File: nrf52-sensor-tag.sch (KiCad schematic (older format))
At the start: 21 parts, among them IC1 ISP1807-LR-RS, IC2 MAX44009EDT+T, J1 Conn_01x06_Male, U1 BME280

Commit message: Finalized layout
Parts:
- removed J1: Conn_01x06_Male, Connector_PinHeader_2.00mm:PinHeader_1x06_P2.00mm_Vertical, symbol Connector:Conn_01x06_Male
- added J3: Conn_01x07_Male, Connector_PinHeader_2.54mm:PinHeader_1x07_P2.54mm_Vertical, symbol Connector:Conn_01x07_Male
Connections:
- net GND: now also J3.4 (Pin_4), J3.5 (Pin_5)
- net Rx: now also J3.6 (Pin_6)
- net SWDCLK: now also J3.1 (Pin_1)
- net SWDIO: now also J3.2 (Pin_2)
- net Tx: now also J3.7 (Pin_7)
- net VCC: now also J3.3 (Pin_3)
- no-connect marks 35 -> 40
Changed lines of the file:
@@
 $EndDescr
-$Comp
-L ISP1807-LR-RS:ISP1807-LR-RS IC1
-U 1 1 601E6B9F
-P 1550 1400
-F 0 "IC1" H 2750 1700 50  0000 C CNN
-F 1 "ISP1807-LR-RS" H 2750 1600 50  0000 C CNN
-F 2 "ISP1807:ISP1807LRRS" H 3700 1500 50  0001 L CNN
-F 3 "https://www.insightsip.com/fichiers_insightsip/pdf/ble/ISP1807/isp_ble_DS1807.pdf" H 3700 1400 50  0001 L CNN
-F 4 "RX TXRX MODULE BT TRC ANT SMD" H 3700 1300 50  0001 L CNN "Description"
-F 5 "1" H 3700 1200 50  0001 L CNN "Height"
-F 6 "Insight SIP" H 3700 1100 50  0001 L CNN "Manufacturer_Name"
-F 7 "ISP1807-LR-RS" H 3700 1000 50  0001 L CNN "Manufacturer_Part_Number"
-F 8 "359-ISP1807-LR-RS" H 3700 900 50  0001 L CNN "Mouser Part Number"
-F 9 "https://www.mouser.co.uk/ProductDetail/Insight-SiP/ISP1807-LR-RS?qs=PqoDHHvF649jBaTuCZQSOQ%3D%3D" H 3700 800 50  0001 L CNN "Mouser Price/Stock"
-F 10 "" H 3700 700 50  0001 L CNN "Arrow Part Number"
-F 11 "" H 3700 600 50  0001 L CNN "Arrow Price/Stock"
-	1    1550 1400
-	1    0    0    -1
-$EndComp
 $Comp
 L power:GND #PWR0101
 U 1 1 6021B8C4
-P 2700 6800
-F 0 "#PWR0101" H 2700 6550 50  0001 C CNN
-F 1 "GND" H 2705 6627 50  0000 C CNN
-F 2 "" H 2700 6800 50  0001 C CNN
-F 3 "" H 2700 6800 50  0001 C CNN
-	1    2700 6800
+P 2700 6850
+F 0 "#PWR0101" H 2700 6600 50  0001 C CNN
+F 1 "GND" H 2705 6677 50  0000 C CNN
+F 2 "" H 2700 6850 50  0001 C CNN
+F 3 "" H 2700 6850 50  0001 C CNN
+	1    2700 6850
 	1    0    0    -1
 $EndComp
@@
 L power:GND #PWR0102
 U 1 1 6020BA24
-P 8600 2550
-F 0 "#PWR0102" H 8600 2300 50  0001 C CNN
-F 1 "GND" H 8605 2377 50  0000 C CNN
-F 2 "" H 8600 2550 50  0001 C CNN
-F 3 "" H 8600 2550 50  0001 C CNN
-	1    8600 2550
+P 8600 2600
+F 0 "#PWR0102" H 8600 2350 50  0001 C CNN
+F 1 "GND" H 8605 2427 50  0000 C CNN
+F 2 "" H 8600 2600 50  0001 C CNN
+F 3 "" H 8600 2600 50  0001 C CNN
+	1    8600 2600
 	1    0    0    -1
 $EndComp
@@
 L power:GND #PWR0103
 U 1 1 6020C669
-P 8800 2550
-F 0 "#PWR0103" H 8800 2300 50  0001 C CNN
-F 1 "GND" H 8805 2377 50  0000 C CNN
-F 2 "" H 8800 2550 50  0001 C CNN
-F 3 "" H 8800 2550 50  0001 C CNN
-	1    8800 2550
+P 8800 2600
+F 0 "#PWR0103" H 8800 2350 50  0001 C CNN
+F 1 "GND" H 8805 2427 50  0000 C CNN
+F 2 "" H 8800 2600 50  0001 C CNN
+F 3 "" H 8800 2600 50  0001 C CNN
+	1    8800 2600
 	1    0    0    -1
 $EndComp
@@
 $EndComp
 Wire Wire Line
-	8600 1300 8800 1300
+	8600 1300 8700 1300
 Wire Wire Line
 	8800 1300 9600 1300
@@
 Connection ~ 8150 4900
 Wire Wire Line
-	8150 4900 8750 4900
+	8150 4900 8450 4900
 NoConn ~ 3850 1500
 NoConn ~ 3850 1700
@@
 Wire Wire Line
 	9600 1300 9900 1300
-$Comp
-L Connector:Conn_01x06_Male J1
-U 1 1 6020A1D2
-P 5200 6650
-F 0 "J1" H 5308 7031 50  0000 C CNN
-F 1 "Conn_01x06_Male" H 5308 6940 50  0000 C CNN
-F 2 "Connector_PinHeader_2.00mm:PinHeader_1x06_P2.00mm_Vertical" H 5200 6650 50  0001 C CNN
-F 3 "~" H 5200 6650 50  0001 C CNN
-	1    5200 6650
-	1    0    0    -1
-$EndComp
 Text Label 5800 6550 2    50   ~ 0
 SWDIO
@@
 $EndComp
 Wire Wire Line
-	5400 6750 6000 6750
+	5400 6750 5500 6750
 Wire Wire Line
 	5800 6650 5400 6650
@@
 Wire Wire Line
 	6000 6800 6000 6750
+Text Label 5800 7050 2    50   ~ 0
+Tx
 Text Label 5800 6950 2    50   ~ 0
-Tx
-Text Label 5800 6850 2    50   ~ 0
 Rx
 Wire Wire Line
-	5800 6850 5400 6850
-Wire Wire Line
 	5800 6950 5400 6950
+Wire Wire Line
+	5800 7050 5400 7050
 Text Label 4400 2600 2    50   ~ 0
 Rx
@@
 	4400 2800 3850 2800
 Wire Wire Line
-	1400 950  2350 950
+	1400 950  2050 950
 Connection ~ 1400 950
 Wire Notes Line
@@
 Text Notes 600  650  0    50   ~ 0
 ISP1807 (nRF52) µC
+$Comp
+L Connector:Conn_01x07_Male J3
+U 1 1 6021CB85
+P 5200 6750
+F 0 "J3" H 5308 7231 50  0000 C CNN
+F 1 "Conn_01x07_Male" H 5308 7140 50  0000 C CNN
+F 2 "Connector_PinHeader_2.54mm:PinHeader_1x07_P2.54mm_Vertical" H 5200 6750 50  0001 C CNN
+F 3 "~" H 5200 6750 50  0001 C CNN
+	1    5200 6750
+	1    0    0    -1
+$EndComp
+Wire Wire Line
+	5400 6850 5500 6850
+Wire Wire Line
+	5500 6850 5500 6750
+Connection ~ 5500 6750
+Wire Wire Line
+	5500 6750 6000 6750
+NoConn ~ 4400 1400
+NoConn ~ 4400 1600
+NoConn ~ 1200 1800
+NoConn ~ 1200 1900
+NoConn ~ 1200 2000
+$Comp
+L power:PWR_FLAG #FLG0101
+U 1 1 6029FC8F
+P 2050 950
+F 0 "#FLG0101" H 2050 1025 50  0001 C CNN
+F 1 "PWR_FLAG" H 2050 1123 50  0000 C CNN
+F 2 "" H 2050 950 50  0001 C CNN
+F 3 "~" H 2050 950 50  0001 C CNN
+	1    2050 950
+	1    0    0    -1
+$EndComp
+Connection ~ 2050 950
+Wire Wire Line
+	2050 950  2350 950
+$Comp
+L power:PWR_FLAG #FLG0102
+U 1 1 602A143F
+P 8450 4900
+F 0 "#FLG0102" H 8450 4975 50  0001 C CNN
+F 1 "PWR_FLAG" H 8450 5073 50  0000 C CNN
+F 2 "" H 8450 4900 50  0001 C CNN
+F 3 "~" H 8450 4900 50  0001 C CNN
+	1    8450 4900
+	1    0    0    -1
+$EndComp
+Connection ~ 8450 4900
+Wire Wire Line
+	8450 4900 8750 4900
+$Comp
+L power:PWR_FLAG #FLG0103
+U 1 1 602A1E76
+P 8700 1300
+F 0 "#FLG0103" H 8700 1375 50  0001 C CNN
+F 1 "PWR_FLAG" H 8700 1473 50  0000 C CNN
+F 2 "" H 8700 1300 50  0001 C CNN
+F 3 "~" H 8700 1300 50  0001 C CNN
+	1    8700 1300
+	1    0    0    -1
+$EndComp
+Connection ~ 8700 1300
+Wire Wire Line
+	8700 1300 8800 1300
+Wire Wire Line
+	8600 2550 8600 2600
+Wire Wire Line
+	8800 2550 8800 2600
+Wire Wire Line
+	2700 6850 2700 6800
+$Comp
+L ISP1807-LR-RS:ISP1807-LR-RS IC1
+U 1 1 601E6B9F
+P 1550 1400
+F 0 "IC1" H 2750 1700 50  0000 C CNN
+F 1 "ISP1807-LR-RS" H 2750 1600 50  0000 C CNN
+F 2 "ISP1807:ISP1807LRRS" H 3700 1500 50  0001 L CNN
+F 3 "https://www.insightsip.com/fichiers_insightsip/pdf/ble/ISP1807/isp_ble_DS1807.pdf" H 3700 1400 50  0001 L CNN
+F 4 "RX TXRX MODULE BT TRC ANT SMD" H 3700 1300 50  0001 L CNN "Description"
+F 5 "1" H 3700 1200 50  0001 L CNN "Height"
+F 6 "Insight SIP" H 3700 1100 50  0001 L CNN "Manufacturer_Name"
+F 7 "ISP1807-LR-RS" H 3700 1000 50  0001 L CNN "Manufacturer_Part_Number"
+F 8 "359-ISP1807-LR-RS" H 3700 900 50  0001 L CNN "Mouser Part Number"
+F 9 "https://www.mouser.co.uk/ProductDetail/Insight-SiP/ISP1807-LR-RS?qs=PqoDHHvF649jBaTuCZQSOQ%3D%3D" H 3700 800 50  0001 L CNN "Mouser Price/Stock"
+F 10 "" H 3700 700 50  0001 L CNN "Arrow Part Number"
+F 11 "" H 3700 600 50  0001 L CNN "Arrow Price/Stock"
+	1    1550 1400
+	1    0    0    -1
+$EndComp
 $EndSCHEMATC

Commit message: Add new alternative sensors
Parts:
- removed IC2: MAX44009EDT+T, MAX44009EDT+T:SON65P200X200X65-7N-D, symbol MAX44009EDT+T:MAX44009EDT+T
- removed U1: BME280, Package_LGA:Bosch_LGA-8_2.5x2.5mm_P0.65mm_ClockwisePinNumbering, symbol Sensor:BME280
- added IC2: VEML6030, VEML6030:VEML6030, symbol VEML6030:VEML6030
- added IC3: MS860702BA01-50, MS860702BA01-50:SON125P300X500X100-8N, symbol MS860702BA01-50:MS860702BA01-50
- added R5: 10R, Resistor_SMD:R_0603_1608Metric, symbol Device:R_Small
- C5: value 0.1uF -> 0.22uF
- C6: value 0.1uF -> 10uF
- C8: value 1uF -> 0.1uF
- R1, R2: value 10k -> 4.7k
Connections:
- net GND: now also IC2.1 (GND), IC3.3 (GND)
- net SCL: now also IC2.5 (SCL), IC3.8 (SCL)
- net SDA: now also IC2.2 (SDA), IC3.7 (SDA)
- net ~INT1: no longer R3.2
- net BME280_VCC renamed SENS1_VCC
- net SENS1_VCC: now also IC3.1 (VDD); no longer C6.1
- net MAX44_VCC renamed SENS2_VCC
- net SENS2_VCC: now also C6.1, R5.1
- new net: IC2.4 (ADD), IC2.6 (VDD), R5.2
- new net INT1: IC2.3 (INT), R3.2
- no-connect marks 40 -> 44
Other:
- note added: "Humid, Temp, Pressure"
- note added: "I2C Address Pressure + Temp: 0x76"
- note added: "I2C Address Relative Humidity: 0x40"
- note added: "I2C Address: 0x48"
- note added: "Light Sensor"
- note removed: "1001010x"
- note removed: "BME280 Humid, Temp, Presure"
- note removed: "I2C Address: 0x4A"
- note removed: "I2C Address: 0x76"
- note removed: "MAX44009 Light Sensor"
- moved on the sheet: JP1, JP2

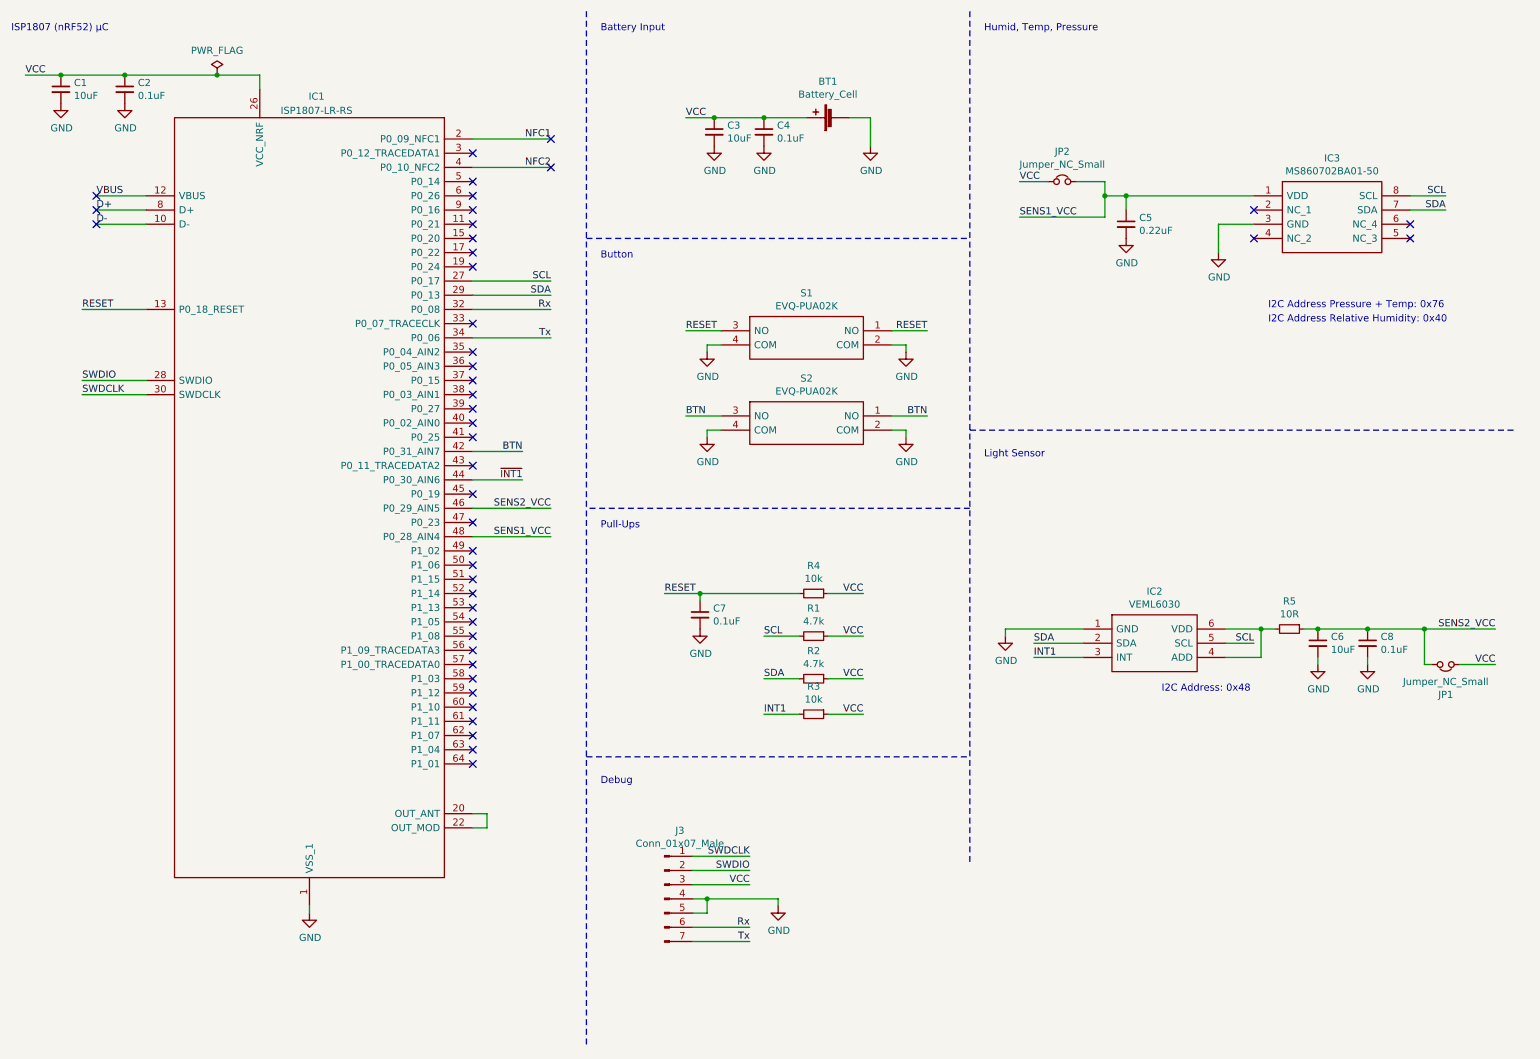
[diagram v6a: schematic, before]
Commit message: Add MS88SF2 nRF52 Module and re-arranged components
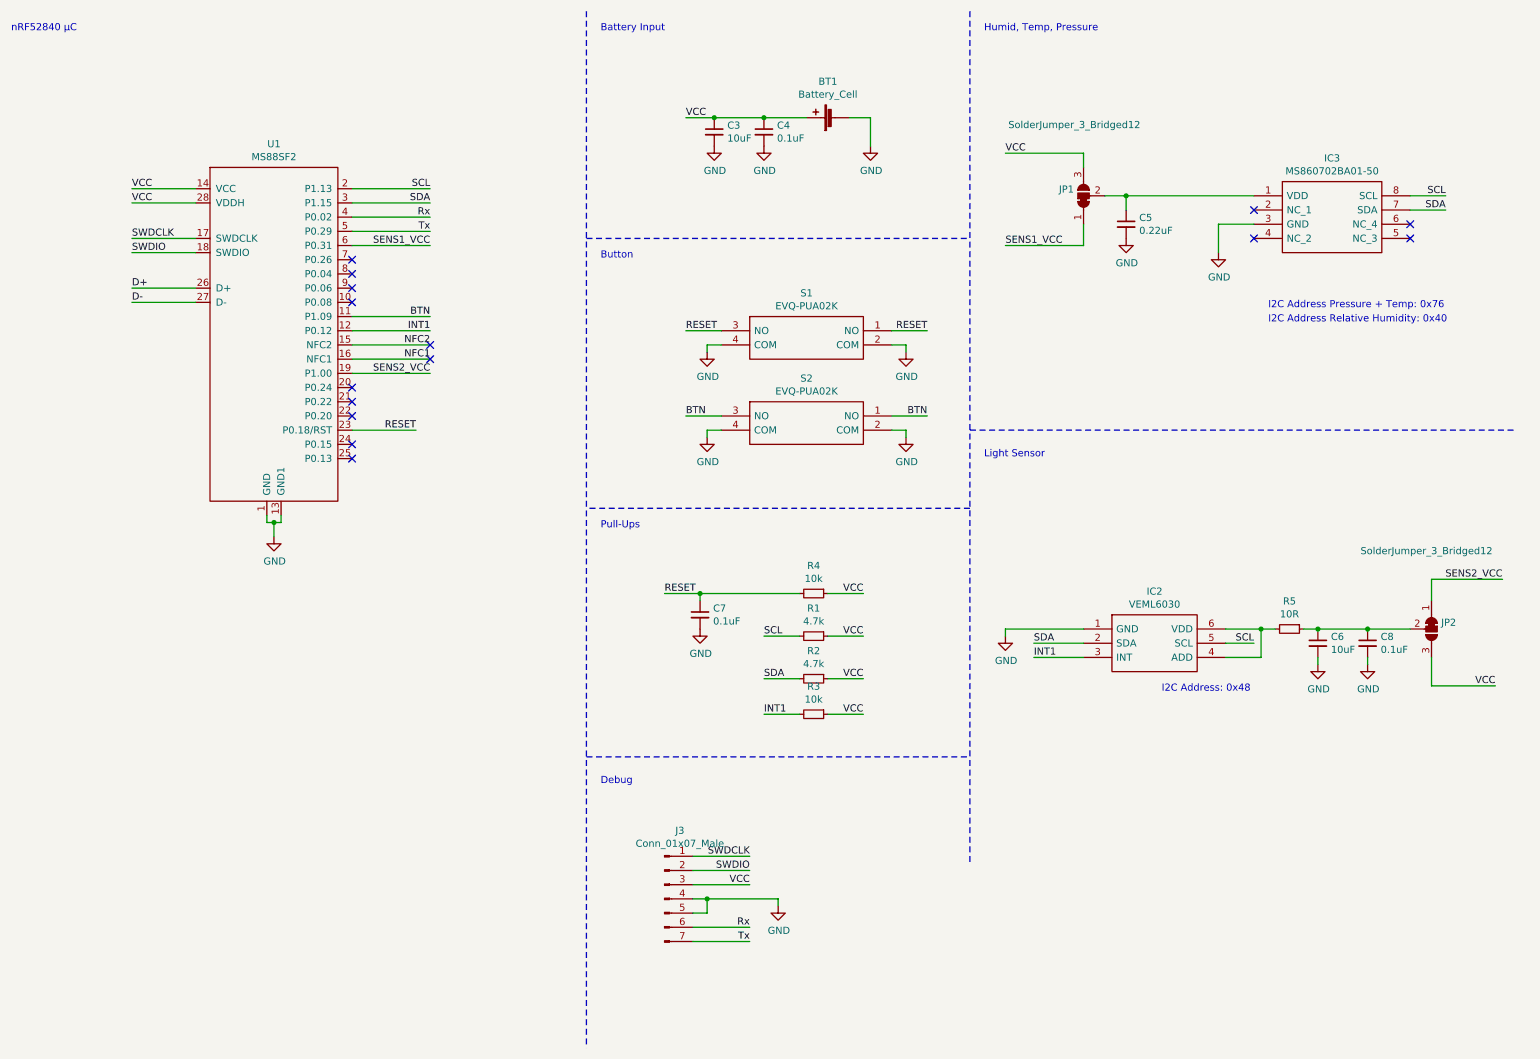
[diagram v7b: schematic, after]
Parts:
- removed C1: 10uF, Capacitor_SMD:C_0603_1608Metric, symbol Device:C_Small
- removed C2: 0.1uF, Capacitor_SMD:C_0603_1608Metric, symbol Device:C_Small
- removed IC1: ISP1807-LR-RS, ISP1807:ISP1807LRRS, symbol ISP1807-LR-RS:ISP1807-LR-RS
- removed JP1, JP2: Jumper_NC_Small, Jumper:SolderJumper-2_P1.3mm_Open_TrianglePad1.0x1.5mm, symbol Device:Jumper_NC_Small
- added JP1, JP2: SolderJumper_3_Bridged12, Jumper:SolderJumper-3_P1.3mm_Bridged12_RoundedPad1.0x1.5mm, symbol Jumper:SolderJumper_3_Bridged12
- added U1: MS88SF2, MS88SF2:MS88SF2, symbol MS88SF2:MS88SF2
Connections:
- net BTN: now also U1.11 (P1.09)
- net D+: now also U1.26 (D+)
- net D-: now also U1.27 (D-)
- net GND: now also U1.1 (GND), U1.13 (GND1)
- net INT1: now also U1.12 (P0.12)
- net NFC1: now also U1.16 (NFC1)
- net NFC2: now also U1.15 (NFC2)
- net RESET: now also U1.23 (P0.18/RST)
- net Rx: now also U1.4 (P0.02)
- net SCL: now also U1.2 (P1.13)
- net SDA: now also U1.3 (P1.15)
- net SENS1_VCC: now also JP1.1 (A), U1.6 (P0.31); no longer C5.1, IC3.1 (VDD)
- net SENS2_VCC: now also JP2.1 (A), U1.19 (P1.00); no longer C6.1, C8.1, R5.1
- net SWDCLK: now also U1.17 (SWDCLK)
- net SWDIO: now also U1.18 (SWDIO)
- net Tx: now also U1.5 (P0.29)
- net VCC: now also JP1.3 (B), JP2.3 (B), U1.14 (VCC), U1.28 (VDDH)
- new net: C6.1, C8.1, JP2.2 (C), R5.1
- new net: C5.1, IC3.1 (VDD), JP1.2 (C)
- no-connect marks 44 -> 15
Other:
- note added: "nRF52840 µC"
- note removed: "ISP1807 (nRF52) µC"
